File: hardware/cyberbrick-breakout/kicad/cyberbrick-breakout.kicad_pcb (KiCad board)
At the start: 2 copper layers, 85 x 70 mm, 33 parts, among them J1 LX, J10 DL_LEFT, J11 DL_RIGHT, J12 DL_DOWN, J13 DR_UP, J14 DR_LEFT, J15 DR_RIGHT, J16 DR_DOWN, J17 SHL1, J18 SHL2, J19 SHR1, J2 LY, J20 SHR2, J21 START, J22 SELECT, J23 HOTKEY, J24 COIN, J3 RX, J4 RY, J6 MCP_BTNS, J7 I2C, J8 PWR_IN, J9 DL_UP, U1A ESP32-C3 top, U1B ESP32-C3 bot

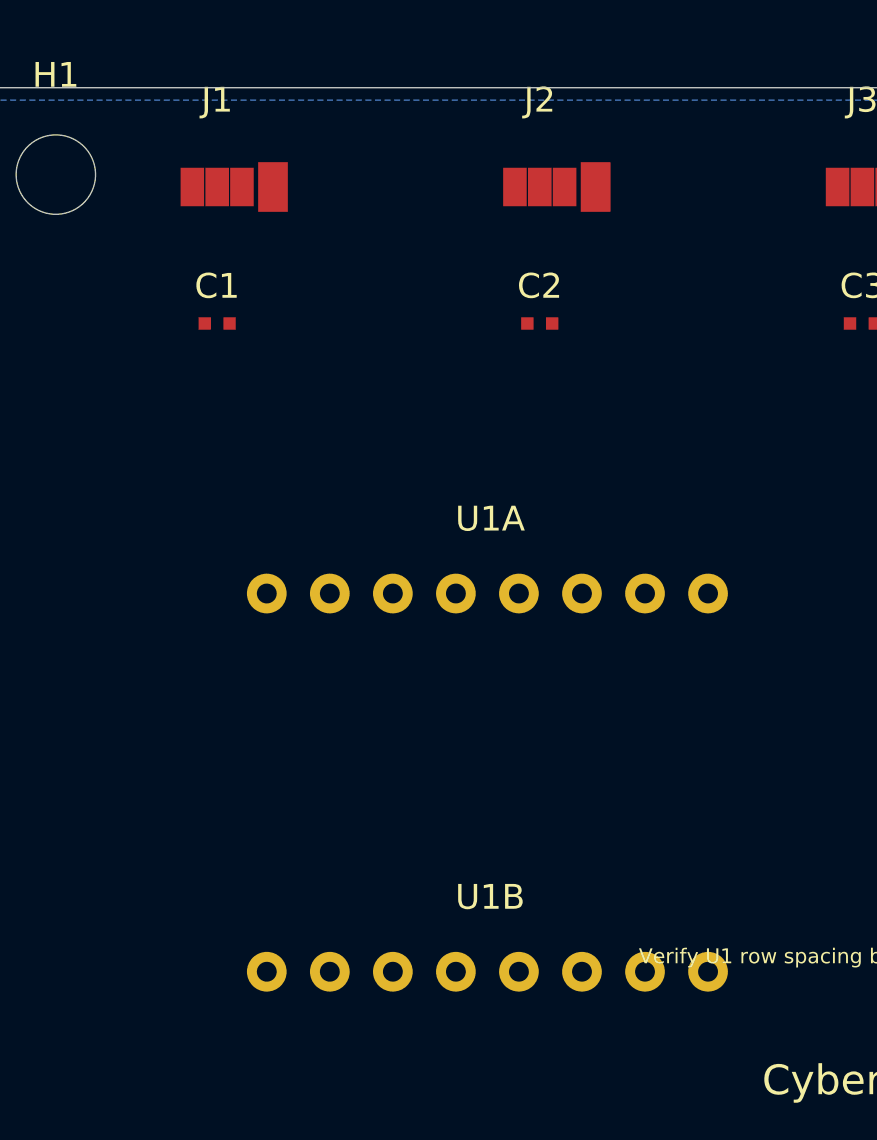
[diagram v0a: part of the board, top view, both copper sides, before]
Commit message: Fix footprint angle: move into (at x y angle) tuple per KiCad 9 format
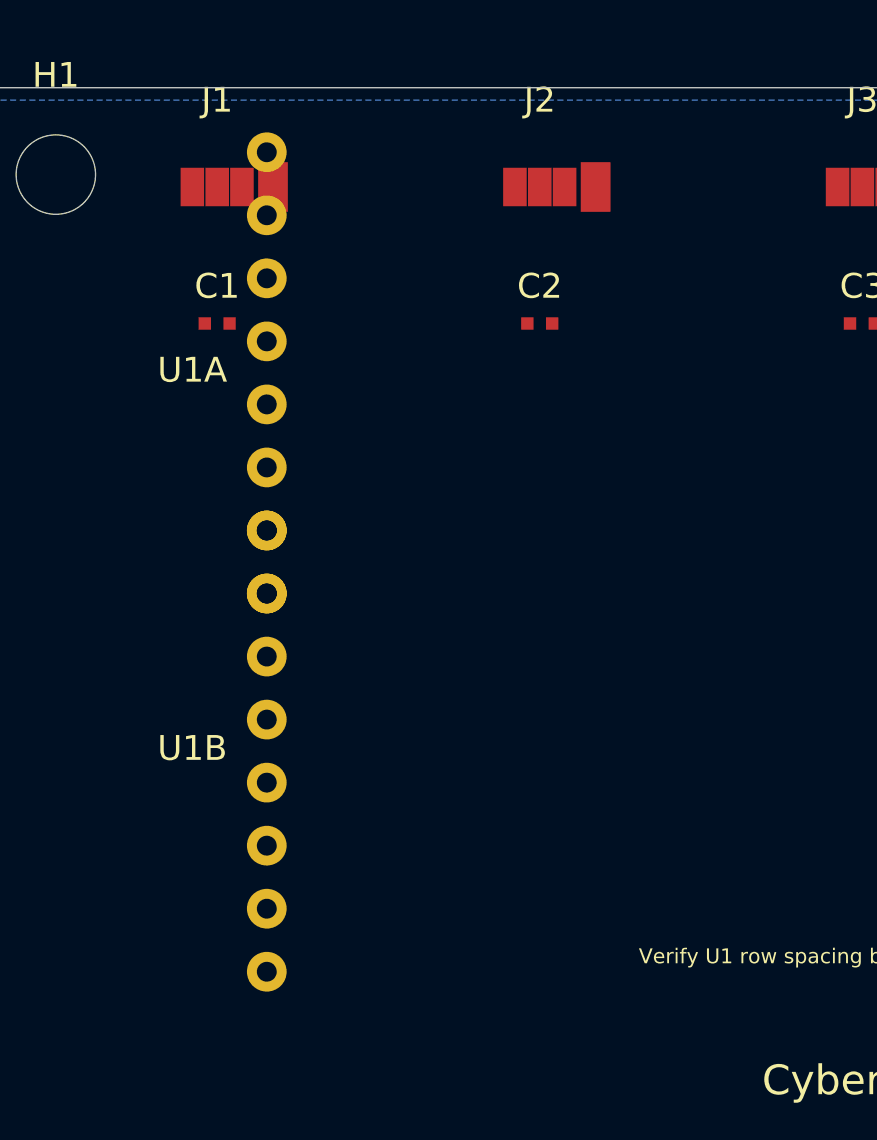
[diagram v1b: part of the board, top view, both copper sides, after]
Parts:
- turned U1A to 90 degrees
- turned U1B to 90 degrees
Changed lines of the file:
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@@
   )
   (footprint "Connector_PinSocket_2.54mm:PinSocket_1x08_P2.54mm_Vertical"
-    (layer "F.Cu") (at 12.0 20.38) (angle 90)
+    (layer "F.Cu") (at 12.0 20.38 90)
     (fp_text reference "U1A" (at 9 -3) (layer "F.SilkS")
       (effects (font (size 1 1) (thickness 0.15))))
@@
   )
   (footprint "Connector_PinSocket_2.54mm:PinSocket_1x08_P2.54mm_Vertical"
-    (layer "F.Cu") (at 12.0 35.62) (angle 90)
+    (layer "F.Cu") (at 12.0 35.62 90)
     (fp_text reference "U1B" (at 9 -3) (layer "F.SilkS")
       (effects (font (size 1 1) (thickness 0.15))))
